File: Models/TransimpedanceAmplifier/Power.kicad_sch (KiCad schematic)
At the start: 3 parts

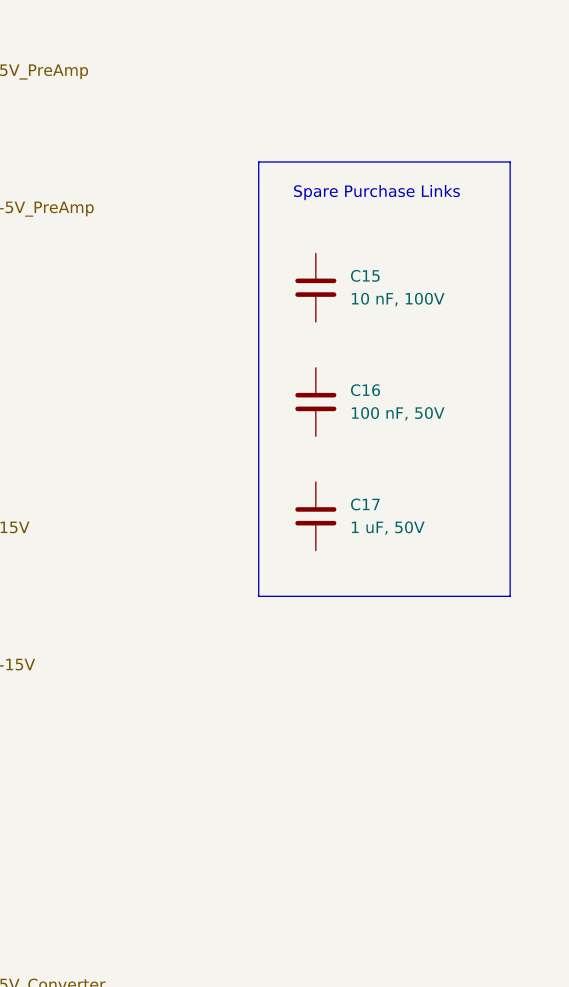
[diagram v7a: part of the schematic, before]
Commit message: Selected a new set of bypass capacitors
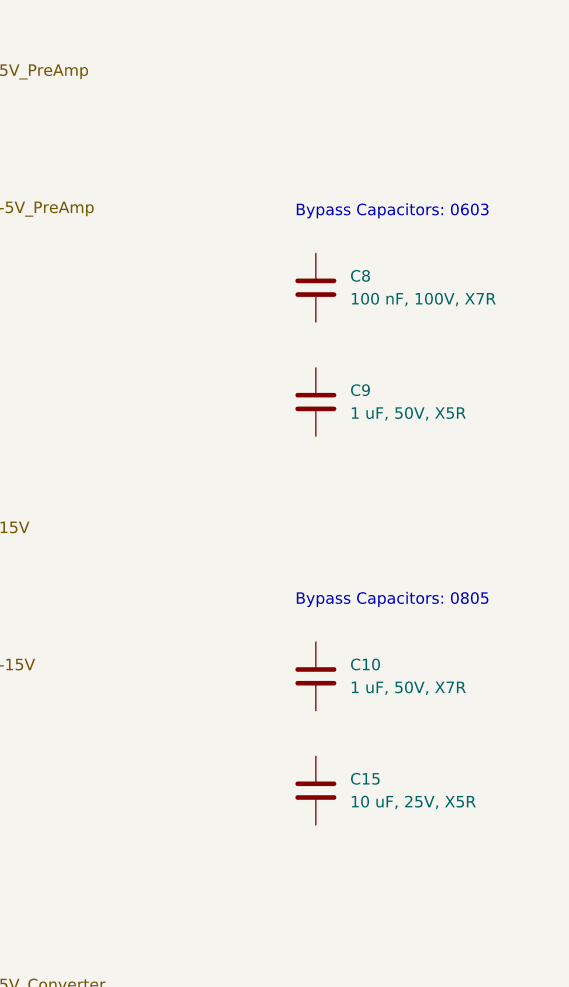
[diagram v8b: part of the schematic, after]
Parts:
- removed C16: 100 nF, 50V, symbol Device:C
- removed C17: 1 uF, 50V, symbol Device:C
- added C10: 1 uF, 50V, X7R, symbol Device:C
- added C8: 100 nF, 100V, X7R, symbol Device:C
- added C9: 1 uF, 50V, X5R, symbol Device:C
- C15: value 10 nF, 100V -> 10 uF, 25V, X5R; Purchase Link https://www.digikey.com/en/products/detail/murata-electronics/GCM188R72A103KA37D/1641655 -> https://www.digikey.com/en/products/detail/murata-electronics/GRM21BR61E106KA73K/4905532
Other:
- note added: "Bypass Capacitors: 0603"
- note added: "Bypass Capacitors: 0805"
- note removed: "Spare Purchase Links"
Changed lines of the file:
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@@
 	(generator_version "9.0")
 	(paper "A4")
-	(rectangle
-		(start 238.76 40.64)
-		(end 266.7 88.9)
-		(stroke
-			(width 0)
-			(type default)
-		)
-		(fill
-			(type none)
-		)
-	)
 	(text "TODO: Include an input-output diode across the\nterminals of all LDO regulators, in line with\nmanufacturer recommendations. We have 470 uF\ncapacitance somewhere.\n\nUse the manufacturer's recommendation of a\nlow-voltage Schottky diode for TLV761. Use the\nrecommendation of a high-voltage diode (1N4002W)\nfor the other regulators. Continue using Schottky\ndiodes to enforce the polarity of the\ninput -> GND differential.\n\nDelete all protection diodes from the schematic.\nDefer the entire cognitive overload of protection\ndiodes until a far-future stage of design, when I\nhave a better understanding of the physical\narrangement of components. And, therefore, a\nmore specific understanding of what transients or\nfault conditions would look like.\n\nI_fault = V_capacitor / ESR"
 		(exclude_from_sim no)
@@
 		)
 	)
+	(text "Bypass Capacitors: 0805"
+		(exclude_from_sim no)
+		(at 242.824 88.646 0)
+		(effects
+			(font
+				(size 1.27 1.27)
+			)
+			(justify left top)
+		)
+	)
 	(text "Maximum Permitted Power Dissipation\nAmbient Temperature: 30°C\n\nLM78L, TO-92\n0.68 W\n0.84 W (heat sinked)\n~158.7°C/W (in a standard test PCB)\n\nLM78, TO-220\n1.78 W\n7.88 W (heat sinked)\n~23.9°C/W (in a standard test PCB)"
 		(exclude_from_sim no)
@@
 		)
 	)
-	(text "Spare Purchase Links"
-		(exclude_from_sim no)
-		(at 242.57 43.434 0)
+	(text "Bypass Capacitors: 0603"
+		(exclude_from_sim no)
+		(at 242.824 45.466 0)
 		(effects
 			(font
@@
 		(dnp no)
 		(fields_autoplaced yes)
-		(property "Reference" "C16"
+		(property "Reference" "C9"
 			(at 248.92 66.0399 0)
 			(effects
@@
 			)
 		)
-		(property "Value" "100 nF, 50V"
+		(property "Value" "1 uF, 50V, X5R"
 			(at 248.92 68.5799 0)
 			(effects
@@
 			)
 		)
-		(property "Purchase Link" "https://www.digikey.com/en/products/detail/murata-electronics/GCM188L81H104KA57J/17846871"
+		(property "Purchase Link" "https://www.digikey.com/en/products/detail/murata-electronics/GRT188R61H105KE13D/5416752"
 			(at 245.11 67.31 0)
 			(effects
@@
 		)
 		(instances
-			(project "TransimpedanceAmplifier"
+			(project ""
 				(path "/ec9f2ae3-e40d-40eb-9760-2b611ee8efd1/d0ece2d4-5b22-4822-ad0c-e2361683ec3d"
-					(reference "C16")
+					(reference "C9")
 					(unit 1)
 				)
@@
 	(symbol
 		(lib_id "Device:C")
-		(at 245.11 80.01 0)
-		(unit 1)
-		(exclude_from_sim no)
-		(in_bom yes)
-		(on_board yes)
-		(dnp no)
-		(fields_autoplaced yes)
-		(property "Reference" "C17"
-			(at 248.92 78.7399 0)
-			(effects
-				(font
-					(size 1.27 1.27)
-				)
-				(justify left)
-			)
-		)
-		(property "Value" "1 uF, 50V"
-			(at 248.92 81.2799 0)
-			(effects
-				(font
-					(size 1.27 1.27)
-				)
-				(justify left)
-			)
-		)
-		(property "Footprint" ""
-			(at 246.0752 83.82 0)
-			(effects
-				(font
-					(size 1.27 1.27)
-				)
-				(hide yes)
-			)
-		)
-		(property "Datasheet" "~"
-			(at 245.11 80.01 0)
-			(effects
-				(font
-					(size 1.27 1.27)
-				)
-				(hide yes)
-			)
-		)
-		(property "Description" "Unpolarized capacitor"
-			(at 245.11 80.01 0)
-			(effects
-				(font
-					(size 1.27 1.27)
-				)
-				(hide yes)
-			)
-		)
-		(property "Purchase Link" "https://www.digikey.com/en/products/detail/murata-electronics/GRT188R61H105KE13D/5416752"
-			(at 245.11 80.01 0)
-			(effects
-				(font
-					(size 1.27 1.27)
-				)
-				(hide yes)
-			)
-		)
-		(pin "1"
-		)
-		(pin "2"
-		)
-		(instances
-			(project "TransimpedanceAmplifier"
-				(path "/ec9f2ae3-e40d-40eb-9760-2b611ee8efd1/d0ece2d4-5b22-4822-ad0c-e2361683ec3d"
-					(reference "C17")
-					(unit 1)
-				)
-			)
-		)
-	)
-	(symbol
-		(lib_id "Device:C")
-		(at 245.11 54.61 0)
+		(at 245.11 110.49 0)
 		(unit 1)
 		(exclude_from_sim no)
@@
 		(fields_autoplaced yes)
 		(property "Reference" "C15"
-			(at 248.92 53.3399 0)
-			(effects
-				(font
-					(size 1.27 1.27)
-				)
-				(justify left)
-			)
-		)
-		(property "Value" "10 nF, 100V"
-			(at 248.92 55.8799 0)
+			(at 248.92 109.2199 0)
+			(effects
+				(font
+					(size 1.27 1.27)
+				)
+				(justify left)
+			)
+		)
+		(property "Value" "10 uF, 25V, X5R"
+			(at 248.92 111.7599 0)
 			(effects
 				(font
@@
 		)
 		(property "Footprint" ""
-			(at 246.0752 58.42 0)
+			(at 246.0752 114.3 0)
 			(effects
 				(font
@@
 		)
 		(property "Datasheet" "~"
-			(at 245.11 54.61 0)
+			(at 245.11 110.49 0)
 			(effects
 				(font
@@
 		)
 		(property "Description" "Unpolarized capacitor"
-			(at 245.11 54.61 0)
-			(effects
-				(font
-					(size 1.27 1.27)
-				)
-				(hide yes)
-			)
-		)
-		(property "Purchase Link" "https://www.digikey.com/en/products/detail/murata-electronics/GCM188R72A103KA37D/1641655"
-			(at 245.11 54.61 0)
+			(at 245.11 110.49 0)
+			(effects
+				(font
+					(size 1.27 1.27)
+				)
+				(hide yes)
+			)
+		)
+		(property "Purchase Link" "https://www.digikey.com/en/products/detail/murata-electronics/GRM21BR61E106KA73K/4905532"
+			(at 245.11 110.49 0)
 			(effects
 				(font
@@
 		)
 		(instances
-			(project "TransimpedanceAmplifier"
+			(project ""
 				(path "/ec9f2ae3-e40d-40eb-9760-2b611ee8efd1/d0ece2d4-5b22-4822-ad0c-e2361683ec3d"
 					(reference "C15")
 					(unit 1)
 				)
+			)
+		)
+	)
+	(symbol
+		(lib_id "Device:C")
+		(at 245.11 54.61 0)
+		(unit 1)
+		(exclude_from_sim no)
+		(in_bom yes)
+		(on_board yes)
+		(dnp no)
+		(fields_autoplaced yes)
+		(property "Reference" "C8"
+			(at 248.92 53.3399 0)
+			(effects
+				(font
+					(size 1.27 1.27)
+				)
+				(justify left)
+			)
+		)
+		(property "Value" "100 nF, 100V, X7R"
+			(at 248.92 55.8799 0)
+			(effects
+				(font
+					(size 1.27 1.27)
+				)
+				(justify left)
+			)
+		)
+		(property "Footprint" ""
+			(at 246.0752 58.42 0)
+			(effects
+				(font
+					(size 1.27 1.27)
+				)
+				(hide yes)
+			)
+		)
+		(property "Datasheet" "~"
+			(at 245.11 54.61 0)
+			(effects
+				(font
+					(size 1.27 1.27)
+				)
+				(hide yes)
+			)
+		)
+		(property "Description" "Unpolarized capacitor"
+			(at 245.11 54.61 0)
+			(effects
+				(font
+					(size 1.27 1.27)
+				)
+				(hide yes)
+			)
+		)
+		(property "Purchase Link" "https://www.digikey.com/en/products/detail/murata-electronics/GRM188R72A104KA35D/702549"
+			(at 245.11 54.61 0)
+			(effects
+				(font
+					(size 1.27 1.27)
+				)
+				(hide yes)
+			)
+		)
+		(pin "1"
+		)
+		(pin "2"
+		)
+		(instances
+			(project ""
+				(path "/ec9f2ae3-e40d-40eb-9760-2b611ee8efd1/d0ece2d4-5b22-4822-ad0c-e2361683ec3d"
+					(reference "C8")
+					(unit 1)
+				)
+			)
+		)
+	)
+	(symbol
+		(lib_id "Device:C")
+		(at 245.11 97.79 0)
+		(unit 1)
+		(exclude_from_sim no)
+		(in_bom yes)
+		(on_board yes)
+		(dnp no)
+		(fields_autoplaced yes)
+		(property "Reference" "C10"
+			(at 248.92 96.5199 0)
+			(effects
+				(font
+					(size 1.27 1.27)
+				)
+				(justify left)
+			)
+		)
+		(property "Value" "1 uF, 50V, X7R"
+			(at 248.92 99.0599 0)
+			(effects
+				(font
+					(size 1.27 1.27)
+				)
+				(justify left)
+			)
+		)
+		(property "Footprint" ""
+			(at 246.0752 101.6 0)
+			(effects
+				(font
+					(size 1.27 1.27)
+				)
+				(hide yes)
+			)
+		)
+		(property "Datasheet" "~"
+			(at 245.11 97.79 0)
+			(effects
+				(font
+					(size 1.27 1.27)
+				)
+				(hide yes)
+			)
+		)
+		(property "Description" "Unpolarized capacitor"
+			(at 245.11 97.79 0)
+			(effects
+				(font
+					(size 1.27 1.27)
+				)
+				(hide yes)
+			)
+		)
+		(property "Purchase Link" "https://www.digikey.com/en/products/detail/murata-electronics/GRT21BR71H105KE01L/10702345"
+			(at 245.11 97.79 0)
+			(effects
+				(font
+					(size 1.27 1.27)
+				)
+				(hide yes)
+			)
+		)
+		(pin "1"
+		)
+		(pin "2"
+		)
+		(instances
+			(project ""
+				(path "/ec9f2ae3-e40d-40eb-9760-2b611ee8efd1/d0ece2d4-5b22-4822-ad0c-e2361683ec3d"
+					(reference "C10")
+					(unit 1)
+				)
